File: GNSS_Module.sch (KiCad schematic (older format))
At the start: 12 parts, among them J12 GPS Shield, J13 GPS_Trasnmission_Conn, U9 ublox_SAM-M8Q

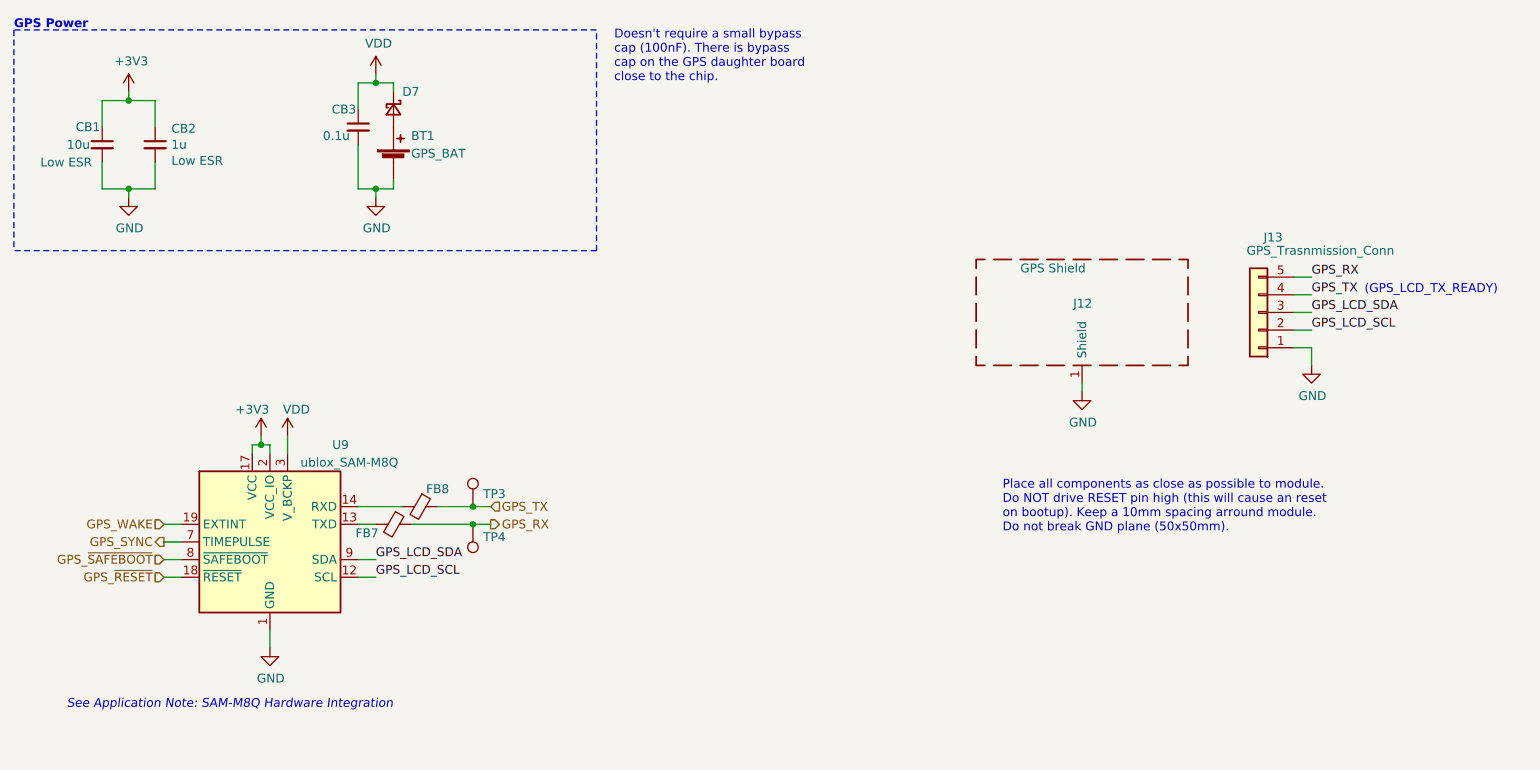
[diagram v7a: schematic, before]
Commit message: Assign footprints for all components
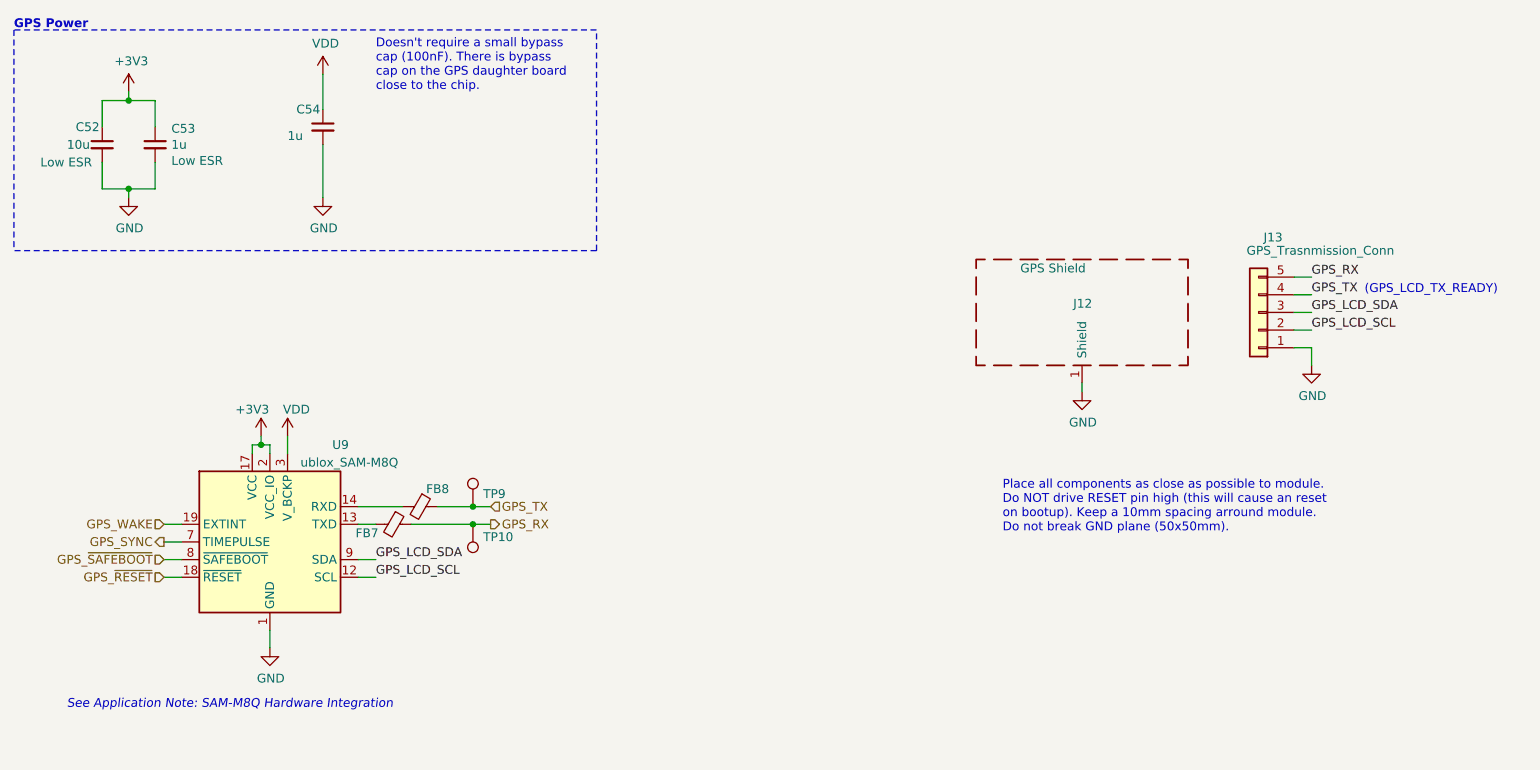
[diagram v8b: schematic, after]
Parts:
- removed BT1: GPS_BAT, symbol Device:Battery_Cell
- removed D7: ~, symbol Device:D_Schottky_Small
- C52: renamed from CB1; footprint (none) -> Capacitor_SMD:C_0805_2012Metric_Pad1.15x1.40mm_HandSolder
- C53: renamed from CB2; footprint (none) -> Capacitor_SMD:C_0603_1608Metric_Pad1.05x0.95mm_HandSolder; MPN (none) -> C0603C105K8RACTU; Mfr. (none) -> KEMET
- C54: renamed from CB3; value 0.1u -> 1u; footprint (none) -> Capacitor_SMD:C_0603_1608Metric_Pad1.05x0.95mm_HandSolder
- FB7, FB8: footprint (none) -> Inductor_SMD:L_0402_1005Metric
- J12: footprint (none) -> RF_Shielding:Wuerth_36503505_50x50mm
- J13: footprint (none) -> Connector_PinHeader_2.54mm:PinHeader_1x05_P2.54mm_Vertical
- TP10: renamed from TP4; footprint (none) -> TestPoint:TestPoint_Pad_D1.0mm
- TP9: renamed from TP3; footprint (none) -> TestPoint:TestPoint_Pad_D1.0mm
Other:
- moved on the sheet: C54
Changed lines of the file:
@@
 P 2250 1800
 AR Path="/5EE05200" Ref="#PWR?"  Part="1"
-AR Path="/5EDF3693/5EE05200" Ref="#PWR0100"  Part="1"
-F 0 "#PWR0100" H 2250 1550 50  0001 C CNN
+AR Path="/5EDF3693/5EE05200" Ref="#PWR0121"  Part="1"
+F 0 "#PWR0121" H 2250 1550 50  0001 C CNN
 F 1 "GND" H 2255 1627 50  0000 C CNN
 F 2 "" H 2250 1800 50  0001 C CNN
@@
 P 2250 1200
 AR Path="/5EE05208" Ref="#PWR?"  Part="1"
-AR Path="/5EDF3693/5EE05208" Ref="#PWR099"  Part="1"
-F 0 "#PWR099" H 2250 1050 50  0001 C CNN
+AR Path="/5EDF3693/5EE05208" Ref="#PWR0120"  Part="1"
+F 0 "#PWR0120" H 2250 1050 50  0001 C CNN
 F 1 "+3V3" H 2265 1373 50  0000 C CNN
 F 2 "" H 2250 1200 50  0001 C CNN
@@
 L power:GND #PWR?
 U 1 1 5EE0520E
-P 3650 1800
+P 3350 1800
 AR Path="/5EE0520E" Ref="#PWR?"  Part="1"
-AR Path="/5EDF3693/5EE0520E" Ref="#PWR0105"  Part="1"
-F 0 "#PWR0105" H 3650 1550 50  0001 C CNN
-F 1 "GND" H 3655 1627 50  0000 C CNN
-F 2 "" H 3650 1800 50  0001 C CNN
-F 3 "" H 3650 1800 50  0001 C CNN
-	1    3650 1800
+AR Path="/5EDF3693/5EE0520E" Ref="#PWR0126"  Part="1"
+F 0 "#PWR0126" H 3350 1550 50  0001 C CNN
+F 1 "GND" H 3355 1627 50  0000 C CNN
+F 2 "" H 3350 1800 50  0001 C CNN
+F 3 "" H 3350 1800 50  0001 C CNN
+	1    3350 1800
 	1    0    0    -1
 $EndComp
@@
 P 3000 3150
 AR Path="/5EE05214" Ref="#PWR?"  Part="1"
-AR Path="/5EDF3693/5EE05214" Ref="#PWR0101"  Part="1"
-F 0 "#PWR0101" H 3000 3000 50  0001 C CNN
+AR Path="/5EDF3693/5EE05214" Ref="#PWR0122"  Part="1"
+F 0 "#PWR0122" H 3000 3000 50  0001 C CNN
 F 1 "+3V3" H 2950 3300 50  0000 C CNN
 F 2 "" H 3000 3150 50  0001 C CNN
@@
 P 3050 4350
 AR Path="/5EE05234" Ref="#PWR?"  Part="1"
-AR Path="/5EDF3693/5EE05234" Ref="#PWR0102"  Part="1"
-F 0 "#PWR0102" H 3050 4100 50  0001 C CNN
+AR Path="/5EDF3693/5EE05234" Ref="#PWR0123"  Part="1"
+F 0 "#PWR0123" H 3050 4100 50  0001 C CNN
 F 1 "GND" H 3055 4177 50  0000 C CNN
 F 2 "" H 3050 4350 50  0001 C CNN
@@
 F 0 "FB7" V 3800 3500 50  0000 C CNN
 F 1 "BLM15HD102SN1" V 3800 4000 50  0001 C CNN
-F 2 "" V 3680 3650 50  0001 C CNN
+F 2 "Inductor_SMD:L_0402_1005Metric" V 3680 3650 50  0001 C CNN
 F 3 "~" H 3750 3650 50  0001 C CNN
 F 4 "BLM15HD102SN1" V 3750 3650 50  0001 C CNN "MPN"
@@
 F 0 "J13" H 8568 2025 50  0000 C CNN
 F 1 "GPS_Trasnmission_Conn" H 8300 2100 50  0000 C CNN
-F 2 "" H 8650 2450 50  0001 C CNN
+F 2 "Connector_PinHeader_2.54mm:PinHeader_1x05_P2.54mm_Vertical" H 8650 2450 50  0001 C CNN
 F 3 "~" H 8650 2450 50  0001 C CNN
 	1    8650 2450
@@
 P 8950 2750
 AR Path="/5EE0524F" Ref="#PWR?"  Part="1"
-AR Path="/5EDF3693/5EE0524F" Ref="#PWR0107"  Part="1"
-F 0 "#PWR0107" H 8950 2500 50  0001 C CNN
+AR Path="/5EDF3693/5EE0524F" Ref="#PWR0128"  Part="1"
+F 0 "#PWR0128" H 8950 2500 50  0001 C CNN
 F 1 "GND" H 8955 2577 50  0000 C CNN
 F 2 "" H 8950 2750 50  0001 C CNN
@@
 Place all components as close as possible to module. \nDo NOT drive RESET pin high (this will cause an reset \non bootup). Keep a 10mm spacing arround module. \nDo not break GND plane (50x50mm).
 $Comp
-L Device:Battery_Cell BT?
-U 1 1 5EE0526D
-P 3750 1600
-AR Path="/5EE0526D" Ref="BT?"  Part="1"
-AR Path="/5EDF3693/5EE0526D" Ref="BT1"  Part="1"
-F 0 "BT1" H 3850 1750 50  0000 L CNN
-F 1 "GPS_BAT" H 3850 1650 50  0000 L CNN
-F 2 "" V 3750 1660 50  0001 C CNN
-F 3 "CR2032" V 3750 1660 50  0001 C CNN
-	1    3750 1600
-	1    0    0    -1
-$EndComp
-$Comp
-L Device:D_Schottky_Small D?
-U 1 1 5EE05273
-P 3750 1300
-AR Path="/5EE05273" Ref="D?"  Part="1"
-AR Path="/5EDF3693/5EE05273" Ref="D7"  Part="1"
-F 0 "D7" V 3650 1350 50  0000 L CNN
-F 1 "~" V 3750 600 50  0000 L CNN
-F 2 "" V 3750 1300 50  0001 C CNN
-F 3 "~" V 3750 1300 50  0001 C CNN
-	1    3750 1300
-	0    1    1    0
-$EndComp
-Wire Wire Line
-	3550 1750 3650 1750
-Wire Wire Line
-	3650 1750 3650 1800
-Wire Wire Line
-	3650 1750 3750 1750
-Wire Wire Line
-	3750 1750 3750 1700
-Connection ~ 3650 1750
-$Comp
-L Device:C_Small CB?
+L Device:C_Small C?
 U 1 1 5EE0527F
 P 2400 1500
-AR Path="/5EE0527F" Ref="CB?"  Part="1"
-AR Path="/5EDF3693/5EE0527F" Ref="CB2"  Part="1"
-F 0 "CB2" H 2492 1591 50  0000 L CNN
+AR Path="/5EE0527F" Ref="C?"  Part="1"
+AR Path="/5EDF3693/5EE0527F" Ref="C53"  Part="1"
+F 0 "C53" H 2492 1591 50  0000 L CNN
 F 1 "1u" H 2492 1500 50  0000 L CNN
-F 2 "" H 2400 1500 50  0001 C CNN
+F 2 "Capacitor_SMD:C_0603_1608Metric_Pad1.05x0.95mm_HandSolder" H 2400 1500 50  0001 C CNN
 F 3 "~" H 2400 1500 50  0001 C CNN
 F 4 "Low ESR" H 2492 1409 50  0000 L CNN "Notes"
+F 5 "C0603C105K8RACTU" H 2400 1500 50  0001 C CNN "MPN"
+F 6 "KEMET" H 2400 1500 50  0001 C CNN "Mfr."
 	1    2400 1500
 	1    0    0    -1
 $EndComp
 $Comp
-L Device:C_Small CB?
+L Device:C_Small C?
 U 1 1 5EE05285
-P 3550 1400
-AR Path="/5EE05285" Ref="CB?"  Part="1"
-AR Path="/5EDF3693/5EE05285" Ref="CB3"  Part="1"
-F 0 "CB3" H 3400 1500 50  0000 L CNN
-F 1 "0.1u" H 3350 1350 50  0000 L CNN
-F 2 "" H 3550 1400 50  0001 C CNN
-F 3 "~" H 3550 1400 50  0001 C CNN
-	1    3550 1400
+P 3350 1400
+AR Path="/5EE05285" Ref="C?"  Part="1"
+AR Path="/5EDF3693/5EE05285" Ref="C54"  Part="1"
+F 0 "C54" H 3200 1500 50  0000 L CNN
+F 1 "1u" H 3150 1350 50  0000 L CNN
+F 2 "Capacitor_SMD:C_0603_1608Metric_Pad1.05x0.95mm_HandSolder" H 3350 1400 50  0001 C CNN
+F 3 "~" H 3350 1400 50  0001 C CNN
+	1    3350 1400
 	1    0    0    -1
 $EndComp
@@
 	2400 1600 2400 1750
 $Comp
-L Device:C_Small CB?
+L Device:C_Small C?
 U 1 1 5EE0528E
 P 2100 1500
-AR Path="/5EE0528E" Ref="CB?"  Part="1"
-AR Path="/5EDF3693/5EE0528E" Ref="CB1"  Part="1"
-F 0 "CB1" H 1950 1600 50  0000 L CNN
+AR Path="/5EE0528E" Ref="C?"  Part="1"
+AR Path="/5EDF3693/5EE0528E" Ref="C52"  Part="1"
+F 0 "C52" H 1950 1600 50  0000 L CNN
 F 1 "10u" H 1900 1500 50  0000 L CNN
-F 2 "" H 2100 1500 50  0001 C CNN
+F 2 "Capacitor_SMD:C_0805_2012Metric_Pad1.15x1.40mm_HandSolder" H 2100 1500 50  0001 C CNN
 F 3 "~" H 2100 1500 50  0001 C CNN
 F 4 "Low ESR" H 1750 1400 50  0000 L CNN "Notes"
@@
 Wire Wire Line
 	2100 1600 2100 1750
-Wire Wire Line
-	3550 1500 3550 1750
-Wire Wire Line
-	3550 1300 3550 1150
-Wire Wire Line
-	3750 1150 3750 1200
 Wire Wire Line
 	2450 3750 2550 3750
@@
 P 7650 2900
 AR Path="/5EE052A0" Ref="#PWR?"  Part="1"
-AR Path="/5EDF3693/5EE052A0" Ref="#PWR0106"  Part="1"
-F 0 "#PWR0106" H 7650 2650 50  0001 C CNN
+AR Path="/5EDF3693/5EE052A0" Ref="#PWR0127"  Part="1"
+F 0 "#PWR0127" H 7650 2650 50  0001 C CNN
 F 1 "GND" H 7655 2727 50  0000 C CNN
 F 2 "" H 7650 2900 50  0001 C CNN
@@
 L power:VDD #PWR?
 U 1 1 5EE052A8
-P 3650 1100
+P 3350 1100
 AR Path="/5EE052A8" Ref="#PWR?"  Part="1"
-AR Path="/5EDF3693/5EE052A8" Ref="#PWR0104"  Part="1"
-F 0 "#PWR0104" H 3650 950 50  0001 C CNN
-F 1 "VDD" H 3665 1273 50  0000 C CNN
-F 2 "" H 3650 1100 50  0001 C CNN
-F 3 "" H 3650 1100 50  0001 C CNN
-	1    3650 1100
-	1    0    0    -1
-$EndComp
-Wire Wire Line
-	3550 1150 3650 1150
-Connection ~ 3650 1150
-Wire Wire Line
-	3650 1150 3750 1150
-Wire Wire Line
-	3650 1100 3650 1150
+AR Path="/5EDF3693/5EE052A8" Ref="#PWR0125"  Part="1"
+F 0 "#PWR0125" H 3350 950 50  0001 C CNN
+F 1 "VDD" H 3365 1273 50  0000 C CNN
+F 2 "" H 3350 1100 50  0001 C CNN
+F 3 "" H 3350 1100 50  0001 C CNN
+	1    3350 1100
+	1    0    0    -1
+$EndComp
 $Comp
 L power:VDD #PWR?
@@
 P 3150 3150
 AR Path="/5EE052B2" Ref="#PWR?"  Part="1"
-AR Path="/5EDF3693/5EE052B2" Ref="#PWR0103"  Part="1"
-F 0 "#PWR0103" H 3150 3000 50  0001 C CNN
+AR Path="/5EDF3693/5EE052B2" Ref="#PWR0124"  Part="1"
+F 0 "#PWR0124" H 3150 3000 50  0001 C CNN
 F 1 "VDD" H 3200 3300 50  0000 C CNN
 F 2 "" H 3150 3150 50  0001 C CNN
@@
 F 0 "FB8" V 3800 3650 50  0000 C CNN
 F 1 "BLM15HD102SN1" V 3950 3900 50  0001 C CNN
-F 2 "" V 3830 3550 50  0001 C CNN
+F 2 "Inductor_SMD:L_0402_1005Metric" V 3830 3550 50  0001 C CNN
 F 3 "~" H 3900 3550 50  0001 C CNN
 F 4 "BLM15HD102SN1" V 3900 3550 50  0001 C CNN "MPN"
@@
 F 0 "J12" H 7600 2500 50  0000 L CNN
 F 1 "GPS Shield" H 7300 2700 50  0000 L CNN
-F 2 "" H 7650 2350 50  0001 C CNN
+F 2 "RF_Shielding:Wuerth_36503505_50x50mm" H 7650 2350 50  0001 C CNN
 F 3 "~" H 7650 2350 50  0001 C CNN
 	1    7650 2450
 	1    0    0    -1
 $EndComp
-Text Notes 5000 1150 0    50   ~ 0
+Text Notes 3650 1200 0    50   ~ 0
 Doesn't require a small bypass \ncap (100nF). There is bypass \ncap on the GPS daughter board \nclose to the chip.
 $Comp
-L Connector:TestPoint TP4
+L Connector:TestPoint TP10
 U 1 1 5F029AD8
 P 4200 3650
-F 0 "TP4" H 4142 3722 50  0000 R CNN
+F 0 "TP10" H 4142 3722 50  0000 R CNN
 F 1 "TestPoint" H 4258 3677 50  0001 L CNN
-F 2 "" H 4400 3650 50  0001 C CNN
+F 2 "TestPoint:TestPoint_Pad_D1.0mm" H 4400 3650 50  0001 C CNN
 F 3 "~" H 4400 3650 50  0001 C CNN
 	1    4200 3650
@@
 	4200 3650 4300 3650
 $Comp
-L Connector:TestPoint TP3
+L Connector:TestPoint TP9
 U 1 1 5F029627
 P 4200 3550
-F 0 "TP3" H 4258 3622 50  0000 L CNN
+F 0 "TP9" H 4258 3622 50  0000 L CNN
 F 1 "TestPoint" H 4258 3577 50  0001 L CNN
-F 2 "" H 4400 3550 50  0001 C CNN
+F 2 "TestPoint:TestPoint_Pad_D1.0mm" H 4400 3550 50  0001 C CNN
 F 3 "~" H 4400 3550 50  0001 C CNN
 	1    4200 3550
@@
 Wire Wire Line
 	4200 3550 4300 3550
+Wire Wire Line
+	3350 1500 3350 1800
+Wire Wire Line
+	3350 1100 3350 1300
 $EndSCHEMATC
